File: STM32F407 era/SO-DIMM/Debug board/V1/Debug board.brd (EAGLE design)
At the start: 91.4 x 41.7 mm, 10 parts, among them J4 FTDI_DEVICE, X1 057-014-1

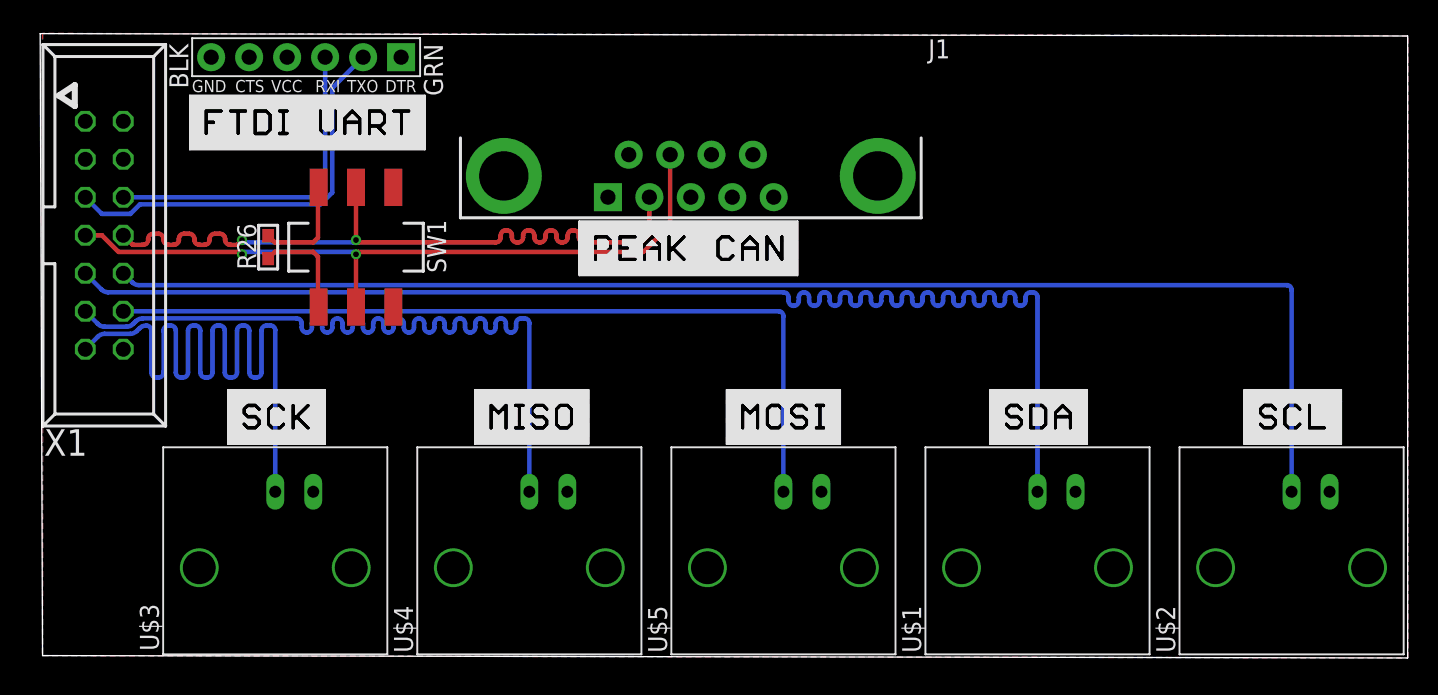
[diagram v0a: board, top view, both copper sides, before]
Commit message: Dashboard done
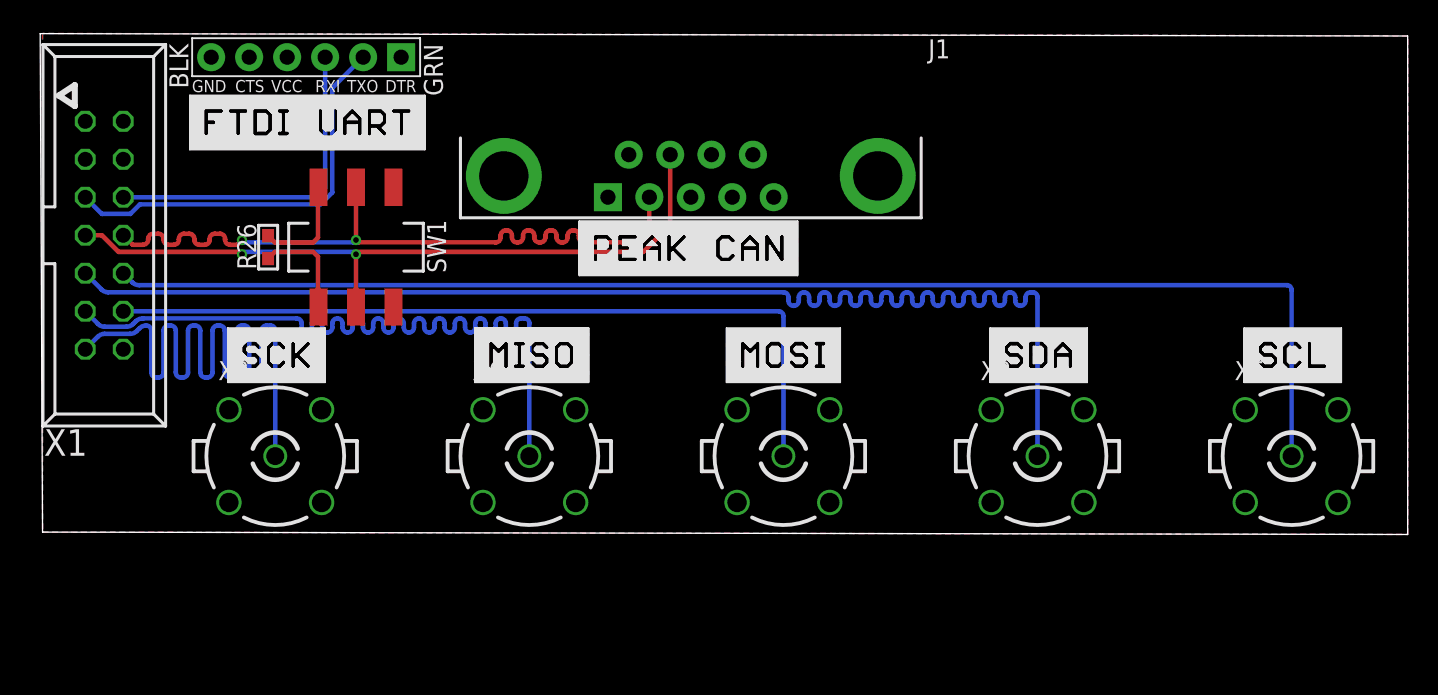
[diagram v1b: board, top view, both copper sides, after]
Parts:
- removed U$1, U$2, U$3, U$4, U$5: BNCPTH, SparkFun-Connectors:BNC
- added X2, X3, X4, X5, X6: BN35N61, con-coax:B35N61
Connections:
- net GND: now also X2.2, X2.3, X2.4, X2.5, X3.2, X3.3, X3.4, X3.5, X4.2, X4.3, X4.4, X4.5, X5.2, X5.3, X5.4, X5.5, X6.2, X6.3, X6.4, X6.5; no longer U$1.GND, U$2.GND, U$3.GND, U$4.GND, U$5.GND
- net MISO: now also X4.1; no longer U$5.S
- net MOSI: now also X6.1; no longer U$4.S
- net SCK: now also X3.1; no longer U$3.S
- net SCL: now also X5.1; no longer U$2.S
- net SDA: now also X2.1; no longer U$1.S
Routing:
- net SDA: track 89.5 -> 87.1 mm
- net MOSI: track 53.6 -> 51.3 mm
- net SCK: track 54.9 -> 52.5 mm
- net SCL: track 92.0 -> 89.6 mm
- net MISO: track 56.0 -> 53.6 mm
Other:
- board size 91.4 x 41.7 mm -> 91.4 x 33.5 mm

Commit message: update to dash, CPU. more work on COM-TC
- Dashboard
Fixed pinout error with overlapping interrupt pins.
Added missing silkscreen marking
- CPU
Added holes for mechanical fastening
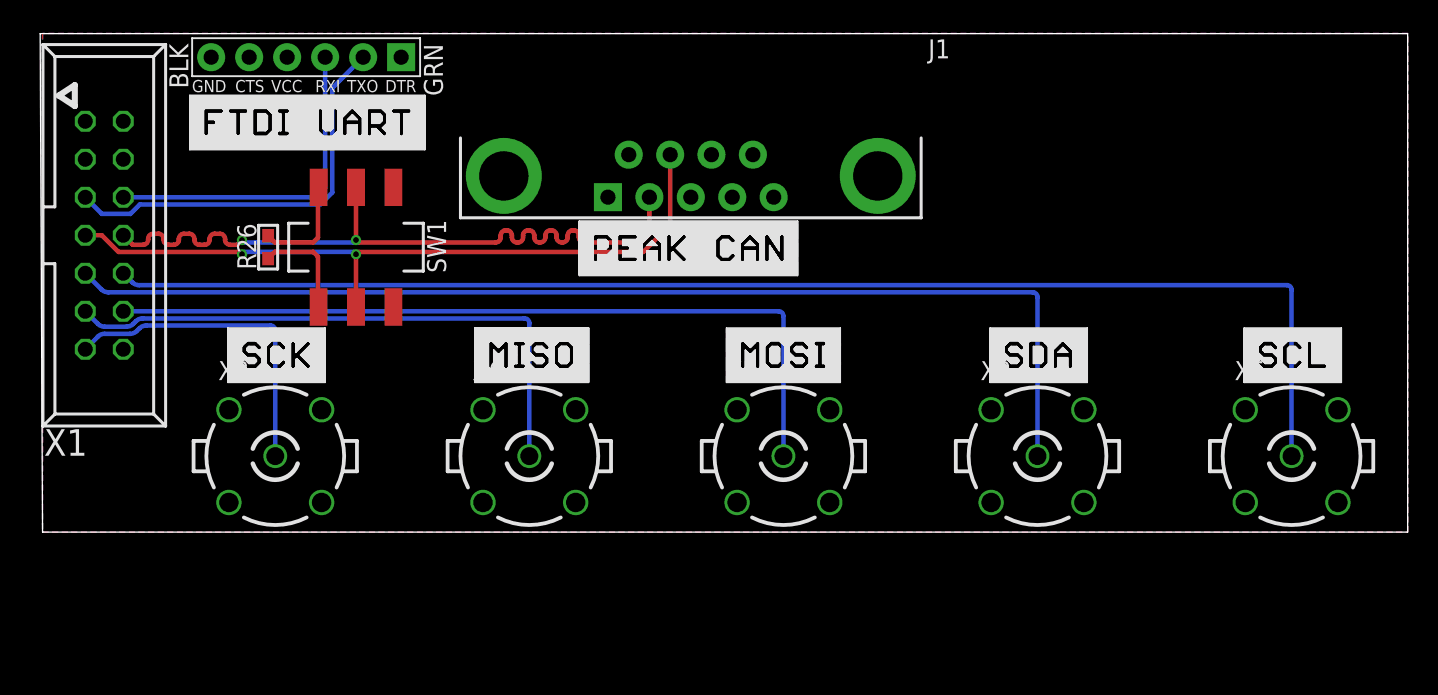
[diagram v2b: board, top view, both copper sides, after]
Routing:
- net SCK: track 52.5 -> 21.8 mm
- net SDA: track 87.1 -> 74.9 mm
- net MOSI: track 51.3 -> 39.2 mm
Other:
- board size 91.4 x 33.5 mm -> 91.4 x 33.3 mm
